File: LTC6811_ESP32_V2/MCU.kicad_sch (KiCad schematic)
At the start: 17 parts, among them J18 B2P-VH-B, J8 JTAG /NC, U8 ESP32-DevKitC V4, U9 LTC6820

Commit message: Add files via upload
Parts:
- removed R35: 806R, Resistor_SMD:R_0603_1608Metric, symbol Device:R_Small
- removed R36, R37: 51R, Resistor_SMD:R_0603_1608Metric, symbol Device:R_Small
- removed R38: 1.2K, Resistor_SMD:R_0603_1608Metric, symbol Device:R_Small
- added R35, R38: 1K, Resistor_SMD:R_0603_1608Metric, symbol Library:R_Small
- added R36, R37: 49.9R, Resistor_SMD:R_0402_1005Metric, symbol Library:R_Small
- C27, C28, C31, C32: symbol Device:C -> Library:C
- C29, C30: footprint Capacitor_SMD:C_0603_1608Metric -> Capacitor_SMD:C_0402_1005Metric; symbol Device:C -> Library:C; Link https://www.digikey.jp/en/products/detail/murata-electronic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 -> https://www.digikey.jp/en/products/detail/kemet/C0402C103K1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; MPN GCM188R72A103KA37D -> C0402C103K1RACAUTO
- J18: symbol Connector_Generic:Conn_01x02 -> Library:Conn_01x02
- J8: symbol Connector_Generic:Conn_01x04 -> Library:Conn_01x04
- R34: symbol Device:R_Small -> Library:R_Small; Link https://www.digikey.jp/en/products/detail/stackpole-electronics-inc/RMCF0603FT10K0/1761235?s=N4IgTCBcDaIEoFkDCAxADANjQZhQFQEY0BpNEAXQF8g -> https://www.digikey.jp/en/products/detail/stackpole-electronics-inc/RMCF0603JT10K0/1758104; MPN RMCF0603FT10K0 -> RMCF0603JT10K0
- R39: symbol Device:R_Small -> Library:R_Small
- TR2: symbol ENNOID:HM2108NL -> Library:HM2108NL
- U8: symbol MCU_Module:ESP32-DevKitC V4 -> Library:ESP32-DevKitC V4_4
- U9: symbol ENNOID:LTC6820 -> Library:LTC6820
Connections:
- net GND: now also R35.1
- net IM: now also R37.1
- net IP: now also R36.2
- net at C30.2: now also R36.1, R37.2
- net at U9.16 (IBIAS): now also R38.2
- net at U9.15 (ICMP): now also R35.2, R38.1

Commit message: Add files via upload
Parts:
- C29, C30: footprint Capacitor_SMD:C_0402_1005Metric -> Capacitor_SMD:C_0603_1608Metric; Link https://www.digikey.jp/en/products/detail/kemet/C0402C103K1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 -> https://www.digikey.jp/en/products/detail/kemet/C0603X103K1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; MPN C0402C103K1RACAUTO -> C0603X103K1RAC3316
- R36, R37: footprint Resistor_SMD:R_0402_1005Metric -> Resistor_SMD:R_0603_1608Metric; Link https://www.digikey.jp/en/products/detail/yageo/RC0402FR-07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 -> https://www.digikey.jp/en/products/detail/panasonic-electro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; MPN RC0402FR-0749R9L -> ERJ-3EKF49R9V
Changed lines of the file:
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@@
 			)
 		)
-		(property "Footprint" "Capacitor_SMD:C_0402_1005Metric"
+		(property "Footprint" "Capacitor_SMD:C_0603_1608Metric"
 			(at 123.19 70.1548 0)
 			(effects
@@
 			)
 		)
-		(property "Datasheet" "https://content.kemet.com/datasheets/KEM_C1023_X7R_AUTO_SMD.pdf"
+		(property "Datasheet" "https://content.kemet.com/datasheets/KEM_X7R_FT_VW_AUDI.pdf"
 			(at 119.38 71.12 0)
 			(effects
@@
 			)
 		)
-		(property "Description" "10000 pF ±10% 100V Ceramic Capacitor X7R 0402 (1005 Metric)"
+		(property "Description" "10000 pF ±10% 100V Ceramic Capacitor X7R 0603 (1608 Metric)"
 			(at 119.38 71.12 0)
 			(effects
@@
 			)
 		)
-		(property "MPN" "C0402C103K1RACAUTO"
+		(property "MPN" "C0603X103K1RAC3316"
 			(at 119.38 71.12 0)
 			(effects
@@
 			)
 		)
-		(property "Link" "https://www.digikey.jp/en/products/detail/kemet/C0402C103K1RACAUTO/19200876"
+		(property "Link" "https://www.digikey.jp/en/products/detail/kemet/C0603X103K1RAC3316/10315782"
 			(at 119.38 71.12 0)
 			(effects
@@
 			)
 		)
-		(property "Footprint" "Capacitor_SMD:C_0402_1005Metric"
+		(property "Footprint" "Capacitor_SMD:C_0603_1608Metric"
 			(at 109.22 70.1548 0)
 			(effects
@@
 			)
 		)
-		(property "Datasheet" "https://content.kemet.com/datasheets/KEM_C1023_X7R_AUTO_SMD.pdf"
+		(property "Datasheet" "https://content.kemet.com/datasheets/KEM_X7R_FT_VW_AUDI.pdf"
 			(at 105.41 71.12 0)
 			(effects
@@
 			)
 		)
-		(property "Description" "10000 pF ±10% 100V Ceramic Capacitor X7R 0402 (1005 Metric)"
+		(property "Description" "10000 pF ±10% 100V Ceramic Capacitor X7R 0603 (1608 Metric)"
 			(at 105.41 71.12 0)
 			(effects
@@
 			)
 		)
-		(property "MPN" "C0402C103K1RACAUTO"
+		(property "MPN" "C0603X103K1RAC3316"
 			(at 105.41 71.12 0)
 			(effects
@@
 			)
 		)
-		(property "Link" "https://www.digikey.jp/en/products/detail/kemet/C0402C103K1RACAUTO/19200876"
+		(property "Link" "https://www.digikey.jp/en/products/detail/kemet/C0603X103K1RAC3316/10315782"
 			(at 105.41 71.12 0)
 			(effects
@@
 			)
 		)
-		(property "Footprint" "Resistor_SMD:R_0402_1005Metric"
+		(property "Footprint" "Resistor_SMD:R_0603_1608Metric"
 			(at 132.08 76.2 0)
 			(effects
@@
 			)
 		)
-		(property "Datasheet" "https://www.yageo.com/upload/media/product/products/datasheet/rchip/PYu-RC_Group_51_RoHS_L_12.pdf"
+		(property "Datasheet" "https://industrial.panasonic.com/cdbs/www-data/pdf/RDA0000/AOA0000C304.pdf"
 			(at 132.08 76.2 0)
 			(effects
@@
 			)
 		)
-		(property "Description" "49.9 Ohms ±1% 0.063W, 1/16W Chip Resistor 0402 (1005 Metric) Moisture Resistant Thick Film"
+		(property "Description" "49.9 Ohms ±1% 0.1W, 1/10W Chip Resistor 0603 (1608 Metric) Automotive AEC-Q200 Thick Film"
 			(at 132.08 76.2 0)
 			(effects
@@
 			)
 		)
-		(property "Link" "https://www.digikey.jp/en/products/detail/yageo/RC0402FR-0749R9L/726621"
+		(property "Link" "https://www.digikey.jp/en/products/detail/panasonic-electronic-components/ERJ-3EKF49R9V/196378"
 			(at 132.08 76.2 0)
 			(effects
@@
 			)
 		)
-		(property "MPN" "RC0402FR-0749R9L"
+		(property "MPN" "ERJ-3EKF49R9V"
 			(at 132.08 76.2 0)
 			(effects
@@
 			)
 		)
-		(property "Footprint" "Resistor_SMD:R_0402_1005Metric"
+		(property "Footprint" "Resistor_SMD:R_0603_1608Metric"
 			(at 132.08 66.04 0)
 			(effects
@@
 			)
 		)
-		(property "Datasheet" "https://www.yageo.com/upload/media/product/products/datasheet/rchip/PYu-RC_Group_51_RoHS_L_12.pdf"
+		(property "Datasheet" "https://industrial.panasonic.com/cdbs/www-data/pdf/RDA0000/AOA0000C304.pdf"
 			(at 132.08 66.04 0)
 			(effects
@@
 			)
 		)
-		(property "Description" "49.9 Ohms ±1% 0.063W, 1/16W Chip Resistor 0402 (1005 Metric) Moisture Resistant Thick Film"
+		(property "Description" "49.9 Ohms ±1% 0.1W, 1/10W Chip Resistor 0603 (1608 Metric) Automotive AEC-Q200 Thick Film"
 			(at 132.08 66.04 0)
 			(effects
@@
 			)
 		)
-		(property "Link" "https://www.digikey.jp/en/products/detail/yageo/RC0402FR-0749R9L/726621"
+		(property "Link" "https://www.digikey.jp/en/products/detail/panasonic-electronic-components/ERJ-3EKF49R9V/196378"
 			(at 132.08 66.04 0)
 			(effects
@@
 			)
 		)
-		(property "MPN" "RC0402FR-0749R9L"
+		(property "MPN" "ERJ-3EKF49R9V"
 			(at 132.08 66.04 0)
 			(effects

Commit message: Add files via upload
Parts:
- removed J18: B2P-VH-B, Connector_JST:JST_VH_B2P-VH-B_1x02_P3.96mm_Vertical, symbol Library:Conn_01x02
- removed J8: JTAG /NC, Connector_PinHeader_2.54mm:PinHeader_1x04_P2.54mm_Vertical, symbol Library:Conn_01x04
- added C68: 100nF/100V, Capacitor_SMD:C_0603_1608Metric, symbol Library:C
- added J20: GPB_0-7, Connector_PinHeader_2.54mm:PinHeader_1x08_P2.54mm_Vertical, symbol Hard_code_serial_num_spi_mcp23s17-rescue:Conn_01x08_Female-Connector
- added J8: Conn_01x08_SPI, Connector_PinHeader_2.54mm:PinHeader_1x08_P2.54mm_Vertical, symbol Hard_code_serial_num_spi_mcp23s17-rescue:Conn_01x08_Female-Connector
- added JP1, JP2, JP3: SolderJumper_3_Bridged12, Jumper:SolderJumper-3_P1.3mm_Open_Pad1.0x1.5mm_NumberLabels, symbol Hard_code_serial_num_spi_mcp23s17-rescue:SolderJumper_3_Bridged12-Jumper
- added R102, R103, R104, R105, R144, R148, R149, R151: 10K, Resistor_SMD:R_0603_1608Metric, symbol Library:R
- added SW1: SW_DIP_x08, Button_Switch_THT:SW_DIP_SPSTx08_Slide_9.78x22.5mm_W7.62mm_P2.54mm, symbol Switch:SW_DIP_x08
- added U1: MCP23S17_SP, Package_DIP:DIP-28_W7.62mm, symbol Interface_Expansion:MCP23S17_SP
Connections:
- net +3V3: now also C68.2, J8.1 (Pin_1), JP1.1 (A), JP2.1 (A), JP3.1 (A), SW1.1, SW1.2, SW1.3, SW1.4, SW1.5, SW1.6, SW1.7, SW1.8, U1.18 (~{RESET}), U1.9 (VDD)
- net GND: now also C68.1, J8.6 (Pin_6), JP1.3 (B), JP2.3 (B), JP3.3 (B), R102.1, R103.1, R104.1, R105.1, R144.1, R148.1, R149.1, R151.1, U1.10 (VSS)
- net IM: now also TR2.1; no longer TR2.3
- net IP: now also TR2.3; no longer TR2.1
- net IPA: now reaches TR2.4
- net IMA: now reaches TR2.6
- net MISO renamed VSPI_MISO
- net MOSI renamed VSPI_MOSI
- net MTCK renamed HSPI_MOSI
- net HSPI_MOSI: now also J8.4 (Pin_4), U1.13 (SI)
- net MTDI renamed HSPI_MISO
- net HSPI_MISO: now also J8.3 (Pin_3), U1.14 (SO)
- net MTDO renamed HSPI_CS
- net HSPI_CS: now also J8.5 (Pin_5), U1.11 (~{CS})
- net MTMS renamed HSPI_SCK
- net HSPI_SCK: now also J8.2 (Pin_2), U1.12 (SCK)
- net SCK renamed VSPI_SCK
- net SS renamed VSPI_CS
- new net: JP3.2 (C), U1.15 (A0)
- new net: R105.2, SW1.13, U1.24 (GPA3)
- new net: R103.2, SW1.15, U1.22 (GPA1)
- new net: R148.2, SW1.11, U1.26 (GPA5)
- new net: J20.1 (Pin_1), U1.1 (GPB0)
- new net: J20.2 (Pin_2), U1.2 (GPB1)
- new net: J20.3 (Pin_3), U1.3 (GPB2)
- new net: J20.4 (Pin_4), U1.4 (GPB3)
- new net: J20.5 (Pin_5), U1.5 (GPB4)
- new net: J20.6 (Pin_6), U1.6 (GPB5)
- new net: J20.7 (Pin_7), U1.7 (GPB6)
- new net: J20.8 (Pin_8), U1.8 (GPB7)
- new net: R149.2, SW1.10, U1.27 (GPA6)
- new net: JP2.2 (C), U1.16 (A1)
- new net: R151.2, SW1.9, U1.28 (GPA7)
- new net: J8.7 (Pin_7), U1.20 (INTA)
- new net: J8.8 (Pin_8), U1.19 (INTB)
- new net: JP1.2 (C), U1.17 (A2)
- new net: R102.2, SW1.16, U1.21 (GPA0)
- new net: R104.2, SW1.14, U1.23 (GPA2)
- new net: R144.2, SW1.12, U1.25 (GPA4)
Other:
- note added: "8: INTB 7: INTA 6: GND 5: CS 4: MOSI 3: MISO 2: SCK 1: 3V3"
- note removed: "For Debugging"

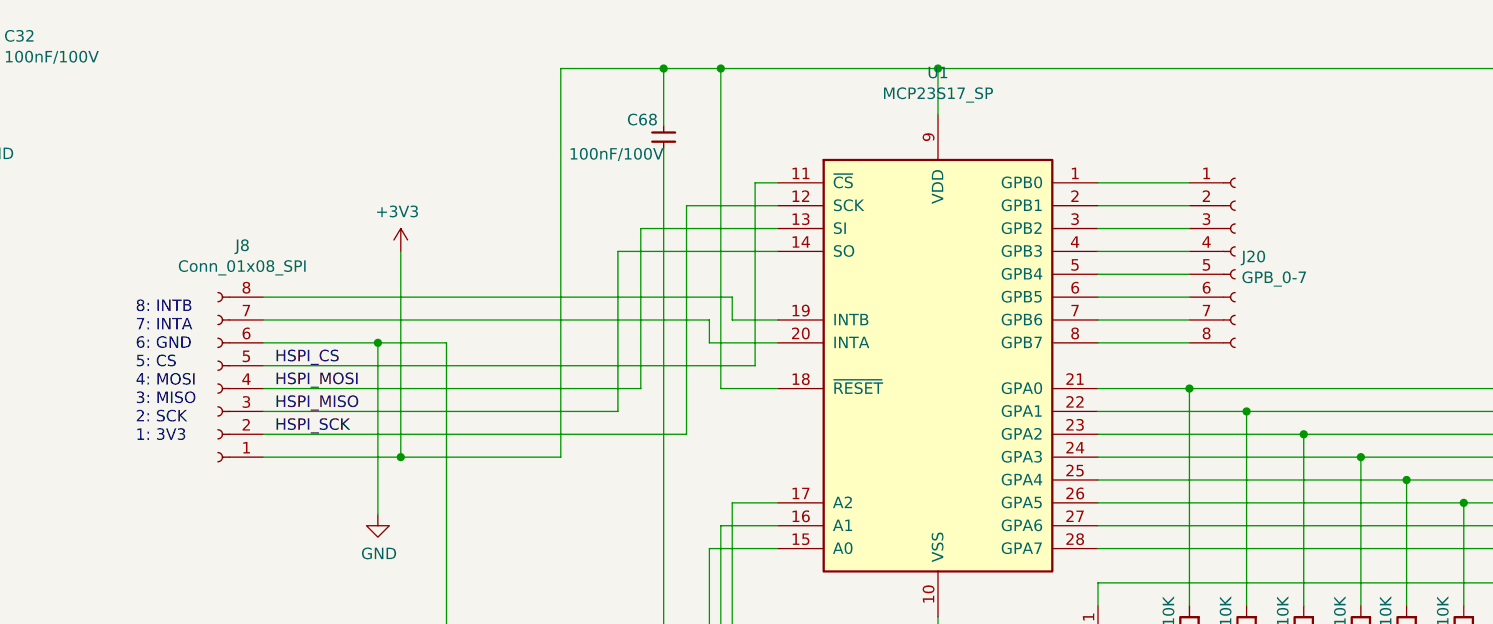
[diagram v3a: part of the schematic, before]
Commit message: Add 8P DIP switch and mcp23s17
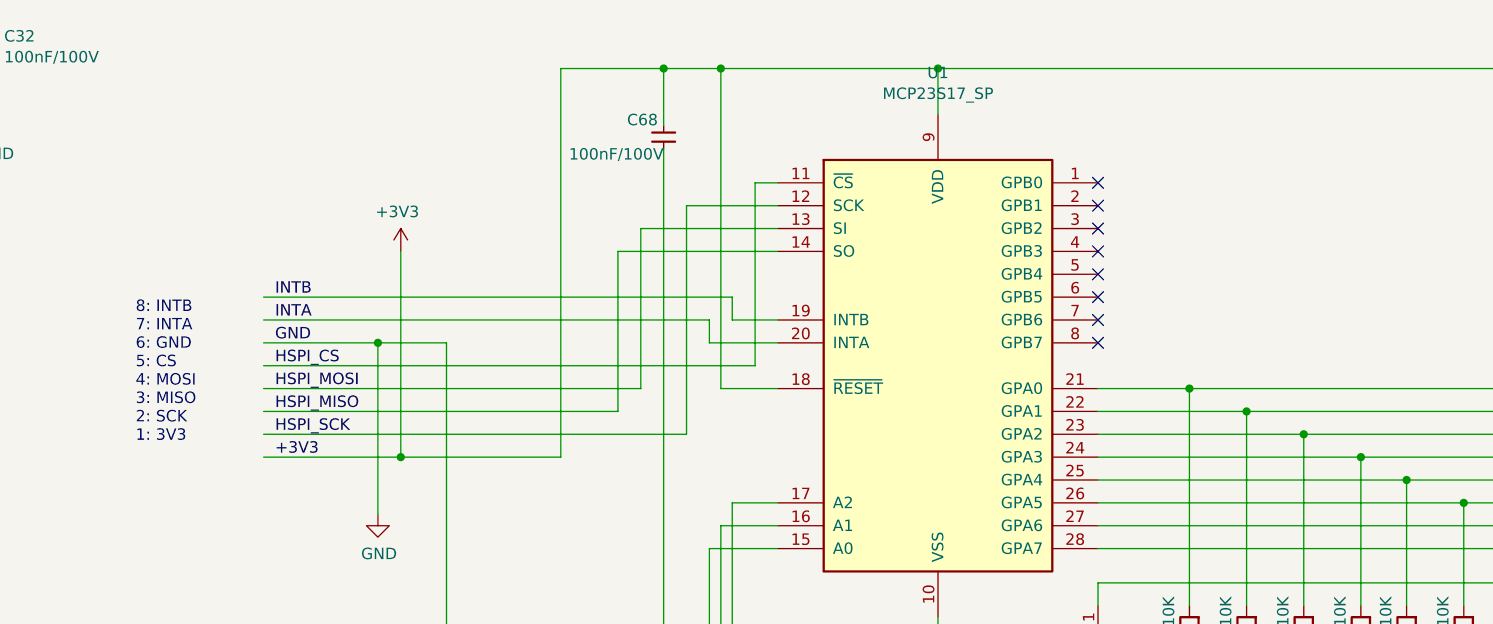
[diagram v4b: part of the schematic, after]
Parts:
- removed J20: GPB_0-7, Connector_PinHeader_2.54mm:PinHeader_1x08_P2.54mm_Vertical, symbol Hard_code_serial_num_spi_mcp23s17-rescue:Conn_01x08_Female-Connector
- removed J8: Conn_01x08_SPI, Connector_PinHeader_2.54mm:PinHeader_1x08_P2.54mm_Vertical, symbol Hard_code_serial_num_spi_mcp23s17-rescue:Conn_01x08_Female-Connector
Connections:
- net INTA: now reaches U1.20 (INTA)
- net INTB: now reaches U1.19 (INTB)
- no-connect marks 22 -> 30

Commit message: Add 8P DIP switch and mcp23s17
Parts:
- JP1, JP2, JP3: symbol Hard_code_serial_num_spi_mcp23s17-rescue:SolderJumper_3_Bridged12-Jumper -> Library:SolderJumper_3_Bridged12-Jumper
- SW1: symbol Switch:SW_DIP_x08 -> Library:SW_DIP_x08
- U1: symbol Interface_Expansion:MCP23S17_SP -> Library:MCP23S17_SP
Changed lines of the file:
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@@
 	)
 	(symbol
-		(lib_id "Hard_code_serial_num_spi_mcp23s17-rescue:SolderJumper_3_Bridged12-Jumper")
+		(lib_id "Library:SolderJumper_3_Bridged12-Jumper")
 		(at 321.31 207.01 270)
 		(unit 1)
@@
 	)
 	(symbol
-		(lib_id "Hard_code_serial_num_spi_mcp23s17-rescue:SolderJumper_3_Bridged12-Jumper")
+		(lib_id "Library:SolderJumper_3_Bridged12-Jumper")
 		(at 321.31 193.04 270)
 		(unit 1)
@@
 	)
 	(symbol
-		(lib_id "Interface_Expansion:MCP23S17_SP")
+		(lib_id "Library:MCP23S17_SP")
 		(at 303.53 147.32 0)
 		(unit 1)
@@
 	)
 	(symbol
-		(lib_id "Hard_code_serial_num_spi_mcp23s17-rescue:GND-power")
+		(lib_id "Library:GND-power")
 		(at 241.3 163.83 0)
 		(unit 1)
@@
 	)
 	(symbol
-		(lib_id "Switch:SW_DIP_x08")
+		(lib_id "Library:SW_DIP_x08")
 		(at 388.62 160.02 0)
 		(mirror y)
@@
 	)
 	(symbol
-		(lib_id "Hard_code_serial_num_spi_mcp23s17-rescue:SolderJumper_3_Bridged12-Jumper")
+		(lib_id "Library:SolderJumper_3_Bridged12-Jumper")
 		(at 321.31 179.07 270)
 		(unit 1)

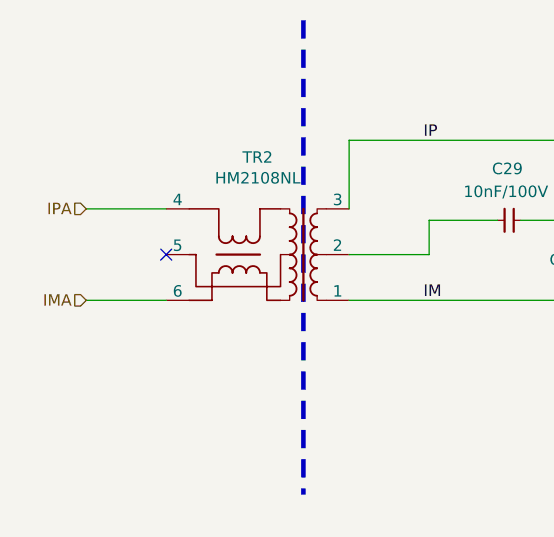
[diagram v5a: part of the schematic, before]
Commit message: Add two positioning holes.
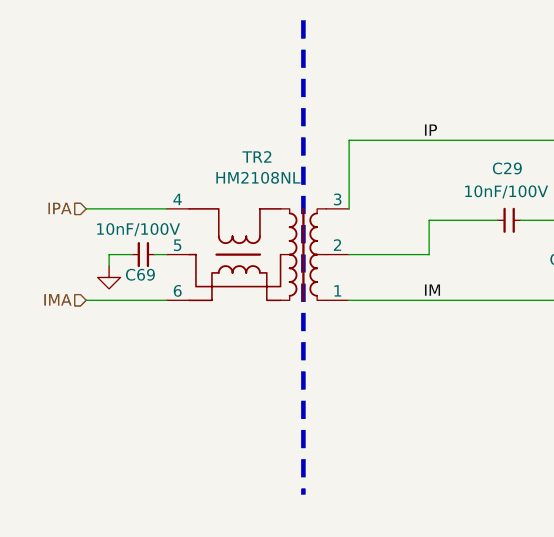
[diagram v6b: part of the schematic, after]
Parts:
- added C69: 10nF/100V, Capacitor_SMD:C_0603_1608Metric, symbol Library:C
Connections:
- net at TR2.5: now also C69.2
- new net GND_PACK: C69.1
- no-connect marks 30 -> 29
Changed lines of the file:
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@@
 	)
 	(no_connect
-		(at 67.31 74.93)
-	)
-	(no_connect
 		(at 142.24 153.67)
 	)
@@
 	(wire
 		(pts
+			(xy 60.96 74.93) (xy 63.5 74.93)
+		)
+		(stroke
+			(width 0)
+			(type default)
+		)
+	)
+	(wire
+		(pts
 			(xy 401.32 114.3) (xy 401.32 149.86)
 		)
@@
 	(wire
 		(pts
+			(xy 60.96 74.93) (xy 60.96 76.2)
+		)
+		(stroke
+			(width 0)
+			(type default)
+		)
+	)
+	(wire
+		(pts
 			(xy 132.08 87.63) (xy 149.86 87.63)
 		)
@@
 	(wire
 		(pts
+			(xy 66.04 74.93) (xy 67.31 74.93)
+		)
+		(stroke
+			(width 0)
+			(type default)
+		)
+	)
+	(wire
+		(pts
 			(xy 228.6 144.78) (xy 241.3 144.78)
 		)
@@
 	)
 	(symbol
+		(lib_id "Library:C")
+		(at 64.77 74.93 90)
+		(unit 1)
+		(exclude_from_sim no)
+		(in_bom yes)
+		(on_board yes)
+		(dnp no)
+		(property "Reference" "C69"
+			(at 62.738 77.216 90)
+			(effects
+				(font
+					(size 1.27 1.27)
+				)
+				(justify right)
+			)
+		)
+		(property "Value" "10nF/100V"
+			(at 59.436 72.136 90)
+			(effects
+				(font
+					(size 1.27 1.27)
+				)
+				(justify right)
+			)
+		)
+		(property "Footprint" "Capacitor_SMD:C_0603_1608Metric"
+			(at 68.58 73.9648 0)
+			(effects
+				(font
+					(size 1.27 1.27)
+				)
+				(hide yes)
+			)
+		)
+		(property "Datasheet" "https://content.kemet.com/datasheets/KEM_X7R_FT_VW_AUDI.pdf"
+			(at 64.77 74.93 0)
+			(effects
+				(font
+					(size 1.27 1.27)
+				)
+				(hide yes)
+			)
+		)
+		(property "Description" "10000 pF ±10% 100V Ceramic Capacitor X7R 0603 (1608 Metric)"
+			(at 64.77 74.93 0)
+			(effects
+				(font
+					(size 1.27 1.27)
+				)
+				(hide yes)
+			)
+		)
+		(property "MPN" "C0603X103K1RAC3316"
+			(at 64.77 74.93 0)
+			(effects
+				(font
+					(size 1.27 1.27)
+				)
+				(hide yes)
+			)
+		)
+		(property "Link" "https://www.digikey.jp/en/products/detail/kemet/C0603X103K1RAC3316/10315782"
+			(at 64.77 74.93 0)
+			(effects
+				(font
+					(size 1.27 1.27)
+				)
+				(hide yes)
+			)
+		)
+		(pin "1"
+		)
+		(pin "2"
+		)
+		(instances
+			(project "LTC6811_ESP32_V2"
+				(path "/6a86ff6f-b159-4c4c-8a40-e732cc82e010/00000000-0000-0000-0000-00005ab72d4d"
+					(reference "C69")
+					(unit 1)
+				)
+			)
+		)
+	)
+	(symbol
 		(lib_id "Library:R")
 		(at 374.65 177.8 180)
@@
 					(unit 1)
 				)
+			)
+		)
+	)
+	(symbol
+		(lib_id "Library:GND_PACK")
+		(at 60.96 76.2 0)
+		(unit 1)
+		(exclude_from_sim no)
+		(in_bom yes)
+		(on_board yes)
+		(dnp no)
+		(property "Reference" "#PWR09"
+			(at 60.96 82.55 0)
+			(effects
+				(font
+					(size 1.27 1.27)
+				)
+				(hide yes)
+			)
+		)
+		(property "Value" "GND_PACK"
+			(at 61.595 79.375 0)
+			(effects
+				(font
+					(size 1.27 1.27)
+				)
+				(hide yes)
+			)
+		)
+		(property "Footprint" ""
+			(at 60.96 76.2 0)
+			(effects
+				(font
+					(size 1.27 1.27)
+				)
+				(hide yes)
+			)
+		)
+		(property "Datasheet" ""
+			(at 60.96 76.2 0)
+			(effects
+				(font
+					(size 1.27 1.27)
+				)
+				(hide yes)
+			)
+		)
+		(property "Description" ""
+			(at 60.96 76.2 0)
+			(effects
+				(font
+					(size 1.27 1.27)
+				)
+				(hide yes)
+			)
+		)
+		(pin "1"
+		)
+		(instances
+			(project "LTC6811_ESP32_V2"
+				(path "/6a86ff6f-b159-4c4c-8a40-e732cc82e010/00000000-0000-0000-0000-00005ab72d4d"
+					(reference "#PWR09")
+					(unit 1)
+				)
